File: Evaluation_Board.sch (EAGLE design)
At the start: 41 parts, among them IC1 MEGA32-A, IC2 FT232RL, IC3 317EMP, J1 DCJ0202

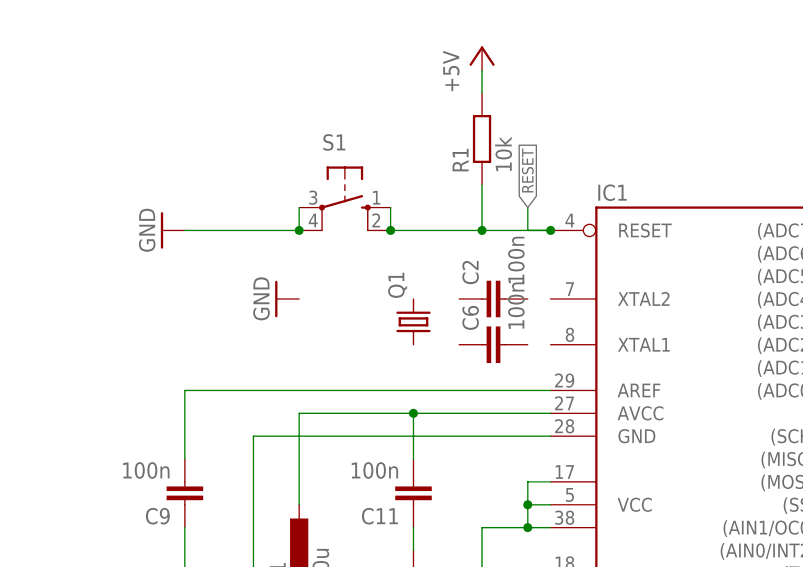
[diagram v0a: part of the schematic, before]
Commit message: Added crystal to layout and changed the values for both load caps.
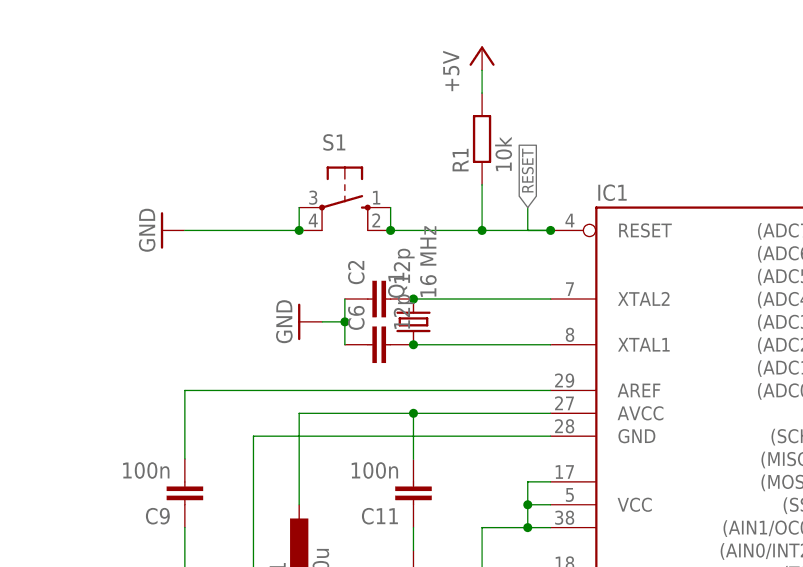
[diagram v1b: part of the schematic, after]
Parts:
- C2, C6: value 100n -> 12p
- Q1: value (none) -> 16 MHz
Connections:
- new net N$17: C2.2, IC1.XTAL2, Q1.2
- new net N$25: C6.2, IC1.XTAL1, Q1.1
- net GND: now also C2.1, C6.1
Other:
- moved on the sheet: C2, C6
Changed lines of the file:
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@@
 <?xml version="1.0" encoding="utf-8"?>
 <!DOCTYPE eagle SYSTEM "eagle.dtd">
-<eagle version="6.4">
+<eagle version="6.5.0">
 <drawing>
 <settings>
@@
 <part name="D2" library="diode" deviceset="DIODE-" device="MINIMELF"/>
 <part name="D3" library="diode" deviceset="DIODE-" device="MINIMELF"/>
-<part name="C2" library="rcl" deviceset="C-EU" device="C0805" value="100n"/>
-<part name="C6" library="rcl" deviceset="C-EU" device="C0805" value="100n"/>
-<part name="Q1" library="crystal" deviceset="CRYSTAL" device="HC49UP"/>
+<part name="C2" library="rcl" deviceset="C-EU" device="C0805" value="12p"/>
+<part name="C6" library="rcl" deviceset="C-EU" device="C0805" value="12p"/>
+<part name="Q1" library="crystal" deviceset="CRYSTAL" device="HC49UP" value="16 MHz"/>
 <part name="SUPPLY22" library="supply1" deviceset="GND" device=""/>
 </parts>
@@
 <instance part="D2" gate="G$1" x="167.64" y="246.38"/>
 <instance part="D3" gate="G$1" x="236.22" y="144.78" rot="R270"/>
-<instance part="C2" gate="G$1" x="78.74" y="190.5" rot="R90"/>
-<instance part="C6" gate="G$1" x="78.74" y="185.42" rot="R90"/>
+<instance part="C2" gate="G$1" x="66.04" y="190.5" rot="R90"/>
+<instance part="C6" gate="G$1" x="66.04" y="185.42" rot="R90"/>
 <instance part="Q1" gate="G$1" x="71.12" y="187.96" rot="R90"/>
-<instance part="SUPPLY22" gate="1" x="55.88" y="190.5" rot="R270"/>
+<instance part="SUPPLY22" gate="1" x="58.42" y="187.96" rot="R270"/>
 </instances>
 <busses>
@@
 <pinref part="C1" gate="G$1" pin="1"/>
 <pinref part="SUPPLY18" gate="1" pin="GND"/>
+</segment>
+<segment>
+<pinref part="C2" gate="G$1" pin="1"/>
+<pinref part="C6" gate="G$1" pin="1"/>
+<wire x1="63.5" y1="190.5" x2="63.5" y2="187.96" width="0.1524" layer="91"/>
+<pinref part="SUPPLY22" gate="1" pin="GND"/>
+<wire x1="63.5" y1="187.96" x2="63.5" y2="185.42" width="0.1524" layer="91"/>
+<wire x1="60.96" y1="187.96" x2="63.5" y2="187.96" width="0.1524" layer="91"/>
+<junction x="63.5" y="187.96"/>
 </segment>
 </net>
@@
 </segment>
 </net>
+<net name="N$17" class="0">
+<segment>
+<pinref part="Q1" gate="G$1" pin="2"/>
+<pinref part="C2" gate="G$1" pin="2"/>
+<pinref part="IC1" gate="G$1" pin="XTAL2"/>
+<wire x1="71.12" y1="190.5" x2="86.36" y2="190.5" width="0.1524" layer="91"/>
+<junction x="71.12" y="190.5"/>
+</segment>
+</net>
+<net name="N$25" class="0">
+<segment>
+<pinref part="Q1" gate="G$1" pin="1"/>
+<pinref part="C6" gate="G$1" pin="2"/>
+<pinref part="IC1" gate="G$1" pin="XTAL1"/>
+<wire x1="86.36" y1="185.42" x2="71.12" y2="185.42" width="0.1524" layer="91"/>
+<junction x="71.12" y="185.42"/>
+</segment>
+</net>

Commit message: Begin of revolution! ;-)
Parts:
- removed R10, R11, R8, R9: 1k, rcl:R-EU_R0805
- added C7: 100n, rcl:C-EUC0805
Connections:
- removed net N$21: IC2.TXD, R8.1
- removed net N$22: IC2.RXD, R9.1
- removed net N$23: IC2.!RTS, R10.1
- removed net N$24: IC2.!CTS, R11.1
- net +5V: now also C7.2
- net CTS: now also IC2.!CTS; no longer R11.2
- net GND: now also C7.1
- net RTS: now also IC2.!RTS; no longer R10.2
- net RX_USB: now also IC2.TXD; no longer R8.2
- net TX_USB: now also IC2.RXD; no longer R9.2
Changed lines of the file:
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@@
 <part name="SUPPLY21" library="supply1" deviceset="+5V" device=""/>
 <part name="SUPPLY23" library="supply1" deviceset="GND" device=""/>
-<part name="R8" library="rcl" deviceset="R-EU_" device="R0805" value="1k"/>
-<part name="R9" library="rcl" deviceset="R-EU_" device="R0805" value="1k"/>
-<part name="R10" library="rcl" deviceset="R-EU_" device="R0805" value="1k"/>
-<part name="R11" library="rcl" deviceset="R-EU_" device="R0805" value="1k"/>
 <part name="SV3" library="pinhead" deviceset="PINHD-1X8" device=""/>
 <part name="SV4" library="pinhead" deviceset="PINHD-1X8" device=""/>
@@
 <part name="Q1" library="crystal" deviceset="CRYSTAL" device="HC49UP" value="16 MHz"/>
 <part name="SUPPLY22" library="supply1" deviceset="GND" device=""/>
+<part name="C7" library="rcl" deviceset="C-EU" device="C0805" value="100n"/>
 </parts>
 <sheets>
@@
 <instance part="SUPPLY21" gate="1" x="320.04" y="177.8"/>
 <instance part="SUPPLY23" gate="1" x="243.84" y="134.62"/>
-<instance part="R8" gate="G$1" x="304.8" y="195.58"/>
-<instance part="R9" gate="G$1" x="314.96" y="193.04"/>
-<instance part="R10" gate="G$1" x="327.66" y="190.5"/>
-<instance part="R11" gate="G$1" x="337.82" y="187.96"/>
 <instance part="SV3" gate="A" x="190.5" y="190.5"/>
 <instance part="SV4" gate="A" x="190.5" y="142.24"/>
@@
 <instance part="Q1" gate="G$1" x="71.12" y="187.96" rot="R90"/>
 <instance part="SUPPLY22" gate="1" x="58.42" y="187.96" rot="R270"/>
+<instance part="C7" gate="G$1" x="76.2" y="144.78" rot="R180"/>
 </instances>
 <busses>
@@
 <wire x1="86.36" y1="157.48" x2="81.28" y2="157.48" width="0.1524" layer="91"/>
 <junction x="81.28" y="157.48"/>
-<wire x1="81.28" y1="134.62" x2="66.04" y2="134.62" width="0.1524" layer="91"/>
+<wire x1="81.28" y1="134.62" x2="76.2" y2="134.62" width="0.1524" layer="91"/>
 <junction x="66.04" y="134.62"/>
 <pinref part="IC1" gate="G$1" pin="GND2"/>
+<wire x1="76.2" y1="134.62" x2="66.04" y2="134.62" width="0.1524" layer="91"/>
 <wire x1="86.36" y1="154.94" x2="81.28" y2="154.94" width="0.1524" layer="91"/>
 <junction x="81.28" y="154.94"/>
+<pinref part="C7" gate="G$1" pin="1"/>
+<wire x1="76.2" y1="142.24" x2="76.2" y2="134.62" width="0.1524" layer="91"/>
+<junction x="76.2" y="134.62"/>
 </segment>
 <segment>
@@
 <wire x1="78.74" y1="165.1" x2="78.74" y2="154.94" width="0.1524" layer="91"/>
 <junction x="83.82" y="165.1"/>
-<wire x1="78.74" y1="154.94" x2="66.04" y2="154.94" width="0.1524" layer="91"/>
+<wire x1="78.74" y1="154.94" x2="76.2" y2="154.94" width="0.1524" layer="91"/>
 <junction x="66.04" y="154.94"/>
 <pinref part="SUPPLY16" gate="1" pin="+5V"/>
+<wire x1="76.2" y1="154.94" x2="66.04" y2="154.94" width="0.1524" layer="91"/>
 <wire x1="58.42" y1="152.4" x2="58.42" y2="154.94" width="0.1524" layer="91"/>
 <junction x="58.42" y="154.94"/>
+<pinref part="C7" gate="G$1" pin="2"/>
+<wire x1="76.2" y1="149.86" x2="76.2" y2="154.94" width="0.1524" layer="91"/>
+<junction x="76.2" y="154.94"/>
 </segment>
 <segment>
@@
 </segment>
 </net>
-<net name="N$21" class="0">
-<segment>
-<pinref part="IC2" gate="1" pin="TXD"/>
-<wire x1="289.56" y1="187.96" x2="294.64" y2="187.96" width="0.1524" layer="91"/>
-<wire x1="294.64" y1="187.96" x2="294.64" y2="195.58" width="0.1524" layer="91"/>
-<pinref part="R8" gate="G$1" pin="1"/>
-<wire x1="294.64" y1="195.58" x2="299.72" y2="195.58" width="0.1524" layer="91"/>
-</segment>
-</net>
-<net name="N$22" class="0">
-<segment>
-<pinref part="IC2" gate="1" pin="RXD"/>
-<wire x1="289.56" y1="185.42" x2="297.18" y2="185.42" width="0.1524" layer="91"/>
-<wire x1="297.18" y1="185.42" x2="297.18" y2="193.04" width="0.1524" layer="91"/>
-<pinref part="R9" gate="G$1" pin="1"/>
-<wire x1="297.18" y1="193.04" x2="309.88" y2="193.04" width="0.1524" layer="91"/>
-</segment>
-</net>
-<net name="N$23" class="0">
-<segment>
-<pinref part="IC2" gate="1" pin="!RTS"/>
-<wire x1="289.56" y1="182.88" x2="299.72" y2="182.88" width="0.1524" layer="91"/>
-<wire x1="299.72" y1="182.88" x2="299.72" y2="190.5" width="0.1524" layer="91"/>
-<wire x1="299.72" y1="190.5" x2="322.58" y2="190.5" width="0.1524" layer="91"/>
-<pinref part="R10" gate="G$1" pin="1"/>
-</segment>
-</net>
-<net name="N$24" class="0">
-<segment>
-<pinref part="IC2" gate="1" pin="!CTS"/>
-<wire x1="289.56" y1="180.34" x2="302.26" y2="180.34" width="0.1524" layer="91"/>
-<wire x1="302.26" y1="180.34" x2="302.26" y2="187.96" width="0.1524" layer="91"/>
-<wire x1="302.26" y1="187.96" x2="332.74" y2="187.96" width="0.1524" layer="91"/>
-<pinref part="R11" gate="G$1" pin="1"/>
-</segment>
-</net>
 <net name="TX_USB" class="0">
 <segment>
@@
 </segment>
 <segment>
-<pinref part="R9" gate="G$1" pin="2"/>
-<wire x1="320.04" y1="193.04" x2="340.36" y2="193.04" width="0.1524" layer="91"/>
+<wire x1="297.18" y1="193.04" x2="340.36" y2="193.04" width="0.1524" layer="91"/>
 <label x="340.36" y="193.04" size="1.27" layer="95" xref="yes"/>
+<pinref part="IC2" gate="1" pin="RXD"/>
+<wire x1="289.56" y1="185.42" x2="297.18" y2="185.42" width="0.1524" layer="91"/>
+<wire x1="297.18" y1="185.42" x2="297.18" y2="193.04" width="0.1524" layer="91"/>
 </segment>
 <segment>
@@
 </segment>
 <segment>
-<pinref part="R8" gate="G$1" pin="2"/>
-<wire x1="309.88" y1="195.58" x2="335.28" y2="195.58" width="0.1524" layer="91"/>
+<wire x1="294.64" y1="195.58" x2="335.28" y2="195.58" width="0.1524" layer="91"/>
 <label x="335.28" y="195.58" size="1.27" layer="95" xref="yes"/>
+<pinref part="IC2" gate="1" pin="TXD"/>
+<wire x1="289.56" y1="187.96" x2="294.64" y2="187.96" width="0.1524" layer="91"/>
+<wire x1="294.64" y1="187.96" x2="294.64" y2="195.58" width="0.1524" layer="91"/>
 </segment>
 <segment>
@@
 <net name="RTS" class="0">
 <segment>
-<pinref part="R10" gate="G$1" pin="2"/>
-<wire x1="332.74" y1="190.5" x2="345.44" y2="190.5" width="0.1524" layer="91"/>
 <label x="345.44" y="190.5" size="1.27" layer="95" xref="yes"/>
+<pinref part="IC2" gate="1" pin="!RTS"/>
+<wire x1="289.56" y1="182.88" x2="299.72" y2="182.88" width="0.1524" layer="91"/>
+<wire x1="299.72" y1="182.88" x2="299.72" y2="190.5" width="0.1524" layer="91"/>
+<wire x1="299.72" y1="190.5" x2="345.44" y2="190.5" width="0.1524" layer="91"/>
 </segment>
 <segment>
@@
 <net name="CTS" class="0">
 <segment>
-<pinref part="R11" gate="G$1" pin="2"/>
-<wire x1="342.9" y1="187.96" x2="347.98" y2="187.96" width="0.1524" layer="91"/>
 <label x="347.98" y="187.96" size="1.27" layer="95" xref="yes"/>
-</segment>
-<segment>
+<pinref part="IC2" gate="1" pin="!CTS"/>
+<wire x1="289.56" y1="180.34" x2="302.26" y2="180.34" width="0.1524" layer="91"/>
+<wire x1="302.26" y1="180.34" x2="302.26" y2="187.96" width="0.1524" layer="91"/>
+<wire x1="302.26" y1="187.96" x2="347.98" y2="187.96" width="0.1524" layer="91"/>
+</segment>
+<segment>

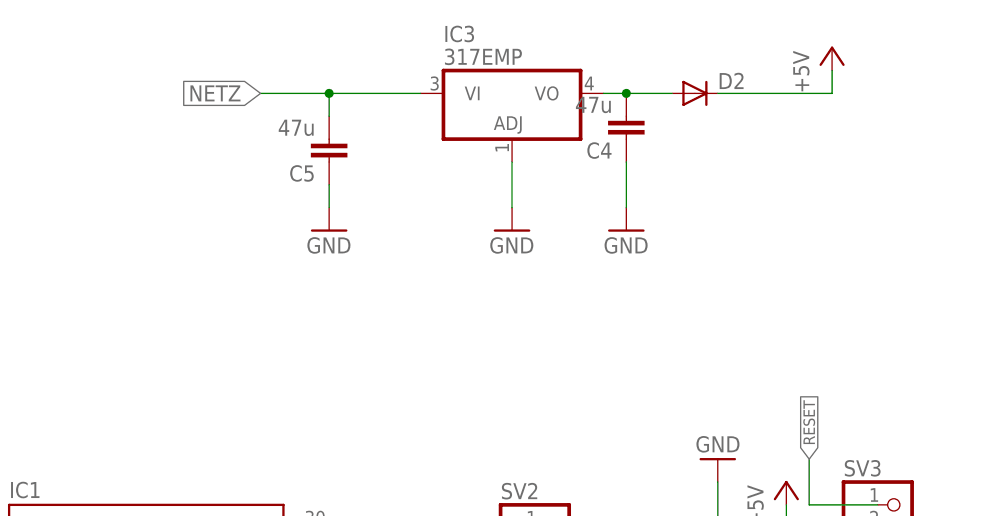
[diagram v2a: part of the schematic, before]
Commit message: No airwires left, implemented crystal layout and removed the resistors on serial line. Removed diode D2 from voltage regulator and placed as anti parallel diode.
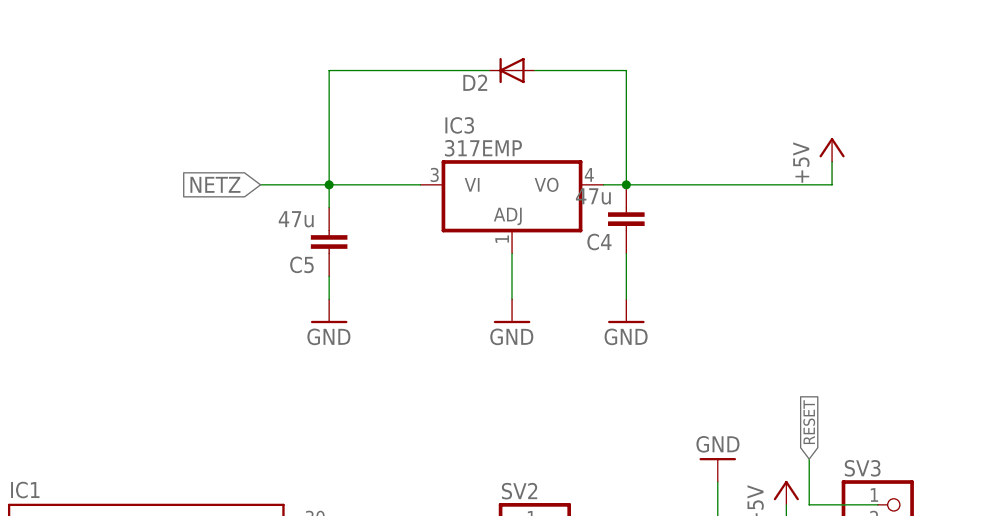
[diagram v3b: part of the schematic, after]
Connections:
- removed net N$2: C4.2, D2.A, IC3.VO
- net +5V: now also C4.2, D2.A, IC3.VO; no longer D2.C
- net NETZ: now also D2.C
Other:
- moved on the sheet: C4, C5, D2, IC3
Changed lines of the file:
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@@
 <instance part="SUPPLY30" gate="1" x="71.12" y="160.02"/>
 <instance part="P+1" gate="1" x="264.16" y="228.6"/>
-<instance part="C4" gate="G$1" x="160.02" y="241.3" rot="R180"/>
-<instance part="C5" gate="G$1" x="127" y="238.76" rot="R180"/>
-<instance part="SUPPLY8" gate="1" x="160.02" y="231.14"/>
-<instance part="SUPPLY9" gate="1" x="127" y="231.14"/>
-<instance part="SUPPLY11" gate="1" x="182.88" y="251.46"/>
+<instance part="C4" gate="G$1" x="160.02" y="231.14" rot="R180"/>
+<instance part="C5" gate="G$1" x="127" y="228.6" rot="R180"/>
+<instance part="SUPPLY8" gate="1" x="160.02" y="220.98"/>
+<instance part="SUPPLY9" gate="1" x="127" y="220.98"/>
+<instance part="SUPPLY11" gate="1" x="182.88" y="241.3"/>
 <instance part="SV5" gate="A" x="152.4" y="142.24"/>
 <instance part="C10" gate="G$1" x="251.46" y="180.34" rot="R180"/>
@@
 <instance part="SUPPLY17" gate="1" x="251.46" y="195.58"/>
 <instance part="SUPPLY3" gate="1" x="78.74" y="218.44"/>
-<instance part="SUPPLY7" gate="1" x="147.32" y="231.14"/>
+<instance part="SUPPLY7" gate="1" x="147.32" y="220.98"/>
 <instance part="JP1" gate="A" x="175.26" y="170.18"/>
-<instance part="IC3" gate="A1" x="147.32" y="243.84"/>
+<instance part="IC3" gate="A1" x="147.32" y="233.68"/>
 <instance part="SUPPLY1" gate="1" x="236.22" y="129.54" rot="R180"/>
 <instance part="C1" gate="G$1" x="86.36" y="48.26" rot="R180"/>
 <instance part="SUPPLY18" gate="1" x="86.36" y="43.18"/>
-<instance part="D2" gate="G$1" x="167.64" y="246.38"/>
+<instance part="D2" gate="G$1" x="147.32" y="248.92" rot="R180"/>
 <instance part="D3" gate="G$1" x="236.22" y="144.78" rot="R270"/>
 <instance part="C2" gate="G$1" x="66.04" y="190.5" rot="R90"/>
@@
 <segment>
 <pinref part="C5" gate="G$1" pin="2"/>
-<wire x1="127" y1="243.84" x2="127" y2="246.38" width="0.1524" layer="91"/>
-<wire x1="127" y1="246.38" x2="119.38" y2="246.38" width="0.1524" layer="91"/>
-<junction x="127" y="246.38"/>
-<label x="119.38" y="246.38" size="1.778" layer="95" rot="R180" xref="yes"/>
-<wire x1="127" y1="246.38" x2="137.16" y2="246.38" width="0.1524" layer="91"/>
+<wire x1="127" y1="233.68" x2="127" y2="236.22" width="0.1524" layer="91"/>
+<wire x1="127" y1="236.22" x2="119.38" y2="236.22" width="0.1524" layer="91"/>
+<junction x="127" y="236.22"/>
+<label x="119.38" y="236.22" size="1.778" layer="95" rot="R180" xref="yes"/>
+<wire x1="127" y1="236.22" x2="137.16" y2="236.22" width="0.1524" layer="91"/>
 <pinref part="IC3" gate="A1" pin="VI"/>
+<pinref part="D2" gate="G$1" pin="C"/>
+<wire x1="144.78" y1="248.92" x2="127" y2="248.92" width="0.1524" layer="91"/>
+<wire x1="127" y1="248.92" x2="127" y2="236.22" width="0.1524" layer="91"/>
 </segment>
 </net>
@@
 <segment>
 <pinref part="SUPPLY7" gate="1" pin="GND"/>
-<wire x1="147.32" y1="238.76" x2="147.32" y2="233.68" width="0.1524" layer="91"/>
+<wire x1="147.32" y1="228.6" x2="147.32" y2="223.52" width="0.1524" layer="91"/>
 <pinref part="IC3" gate="A1" pin="ADJ"/>
 </segment>
@@
 <pinref part="C4" gate="G$1" pin="1"/>
 <pinref part="SUPPLY8" gate="1" pin="GND"/>
-<wire x1="160.02" y1="238.76" x2="160.02" y2="233.68" width="0.1524" layer="91"/>
+<wire x1="160.02" y1="228.6" x2="160.02" y2="223.52" width="0.1524" layer="91"/>
 </segment>
 <segment>
@@
 <pinref part="C5" gate="G$1" pin="1"/>
 <pinref part="SUPPLY9" gate="1" pin="GND"/>
-<wire x1="127" y1="236.22" x2="127" y2="233.68" width="0.1524" layer="91"/>
+<wire x1="127" y1="226.06" x2="127" y2="223.52" width="0.1524" layer="91"/>
 </segment>
 <segment>
@@
 </segment>
 <segment>
-<wire x1="182.88" y1="248.92" x2="182.88" y2="246.38" width="0.1524" layer="91"/>
+<wire x1="182.88" y1="238.76" x2="182.88" y2="236.22" width="0.1524" layer="91"/>
 <pinref part="SUPPLY11" gate="1" pin="+5V"/>
-<pinref part="D2" gate="G$1" pin="C"/>
-<wire x1="170.18" y1="246.38" x2="182.88" y2="246.38" width="0.1524" layer="91"/>
+<wire x1="157.48" y1="236.22" x2="160.02" y2="236.22" width="0.1524" layer="91"/>
+<pinref part="IC3" gate="A1" pin="VO"/>
+<pinref part="C4" gate="G$1" pin="2"/>
+<wire x1="160.02" y1="236.22" x2="182.88" y2="236.22" width="0.1524" layer="91"/>
+<junction x="160.02" y="236.22"/>
+<pinref part="D2" gate="G$1" pin="A"/>
+<wire x1="149.86" y1="248.92" x2="160.02" y2="248.92" width="0.1524" layer="91"/>
+<wire x1="160.02" y1="248.92" x2="160.02" y2="236.22" width="0.1524" layer="91"/>
 </segment>
 <segment>
@@
 </segment>
 </net>
-<net name="N$2" class="0">
-<segment>
-<pinref part="D2" gate="G$1" pin="A"/>
-<wire x1="157.48" y1="246.38" x2="160.02" y2="246.38" width="0.1524" layer="91"/>
-<pinref part="IC3" gate="A1" pin="VO"/>
-<pinref part="C4" gate="G$1" pin="2"/>
-<wire x1="160.02" y1="246.38" x2="165.1" y2="246.38" width="0.1524" layer="91"/>
-<junction x="160.02" y="246.38"/>
-</segment>
-</net>
